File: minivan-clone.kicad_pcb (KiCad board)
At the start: 2 copper layers, 247.4 x 75.9 mm, 116 parts, among them CON101 HRO-TYPE-C-31-M-12, K101 KEYSW, K102 KEYSW, K103 KEYSW, K104 KEYSW, K105 KEYSW, K106 KEYSW, K107 KEYSW, K108 KEYSW, K110 KEYSW, K111 KEYSW, K112 KEYSW, K113 KEYSW, K114 KEYSW, K115 KEYSW, K116 KEYSW, K117 KEYSW, K118 KEYSW, K119 KEYSW, K120 KEYSW, K121 KEYSW, K122 KEYSW, K123 KEYSW, K124 KEYSW, K125 KEYSW, K126 KEYSW, K127 KEYSW, K128 KEYSW, K129 KEYSW, K130 KEYSW, K131 KEYSW, K132 KEYSW, K133 KEYSW, K134 KEYSW, K135 KEYSW, K136 KEYSW, K137 KEYSW, K138 KEYSW, K139 KEYSW, K140 KEYSW, K141 KEYSW, K142 KEYSW, K143 KEYSW, K144 KEYSW, K145 KEYSW, K146 KEYSW, K147 KEYSW, K148 KEYSW, SW101 SW_PUSH, U101 ATMEGA32U2, X101 XTAL_GND

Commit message: added icon to pcb
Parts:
- added G***: LOGO, icon:icon, F.Cu at (345.9, 165.1)
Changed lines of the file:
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@@
     (tracks 863)
     (zones 0)
-    (modules 116)
+    (modules 117)
     (nets 84)
   )
@@
     (add_net "Net-(R102-Pad1)")
   )
+  (module icon:icon (layer F.Cu)
+    (at 345.948 165.1)
+    (fp_text reference G*** (at 0 0) (layer F.SilkS) hide
+      (effects (font (size 1.524 1.524) (thickness 0.3)))
+    )
+    (fp_text value LOGO (at 0.75 0) (layer F.SilkS) hide
+      (effects (font (size 1.524 1.524) (thickness 0.3)))
+    )
+    (fp_poly (pts (xy -16.681691 0.453633) (xy -16.67213 1.32069) (xy -16.395957 2.129268) (xy -15.885356 2.816868)
+      (xy -15.216434 3.299082) (xy -14.794581 3.57815) (xy -14.668687 3.834571) (xy -14.671541 3.855207)
+      (xy -14.842051 4.080963) (xy -15.185572 4.143386) (xy -15.624922 4.042535) (xy -15.979205 3.854169)
+      (xy -16.385945 3.485206) (xy -16.734086 3.020855) (xy -16.778041 2.941403) (xy -16.985788 2.316247)
+      (xy -17.061288 1.584014) (xy -17.002025 0.87235) (xy -16.829138 0.350734) (xy -16.600536 -0.074706)
+      (xy -16.681691 0.453633)) (layer Eco2.User) (width 0.01))
+    (fp_poly (pts (xy 8.827697 -3.648363) (xy 9.045453 -3.521941) (xy 9.243273 -3.305469) (xy 9.192998 -3.067425)
+      (xy 9.173564 -3.034339) (xy 8.911681 -2.792098) (xy 8.593301 -2.716115) (xy 8.333057 -2.820437)
+      (xy 8.267906 -2.923358) (xy 8.265608 -3.265696) (xy 8.44141 -3.581057) (xy 8.607893 -3.691062)
+      (xy 8.827697 -3.648363)) (layer Eco2.User) (width 0.01))
+    (fp_poly (pts (xy -0.177583 -3.642129) (xy -0.048558 -3.564181) (xy 0.107123 -3.282951) (xy 0.119269 -3.076015)
+      (xy -0.040312 -2.811696) (xy -0.337821 -2.714246) (xy -0.64642 -2.811993) (xy -0.725358 -2.887381)
+      (xy -0.833872 -3.192888) (xy -0.726542 -3.47272) (xy -0.481677 -3.648569) (xy -0.177583 -3.642129)) (layer Eco2.User) (width 0.01))
+    (fp_poly (pts (xy 11.243235 -1.616568) (xy 11.545267 -1.447253) (xy 11.625766 -1.243258) (xy 11.67212 -0.917693)
+      (xy 12.20691 -1.280611) (xy 12.889803 -1.582854) (xy 13.622875 -1.639094) (xy 14.323873 -1.456975)
+      (xy 14.910544 -1.044138) (xy 14.925771 -1.027997) (xy 15.237885 -0.692982) (xy 15.575119 -1.000173)
+      (xy 16.265855 -1.452416) (xy 17.026616 -1.648439) (xy 17.792864 -1.580315) (xy 18.349285 -1.340875)
+      (xy 18.711707 -1.060091) (xy 18.970212 -0.696074) (xy 19.139809 -0.199258) (xy 19.235508 0.479923)
+      (xy 19.272315 1.391035) (xy 19.274118 1.713437) (xy 19.274118 3.436471) (xy 18.527059 3.436471)
+      (xy 18.527059 1.802668) (xy 18.512977 0.903898) (xy 18.460201 0.251592) (xy 18.352937 -0.205728)
+      (xy 18.175389 -0.519542) (xy 17.911764 -0.74133) (xy 17.713869 -0.847765) (xy 17.298857 -1.001579)
+      (xy 16.920113 -0.999688) (xy 16.606378 -0.920616) (xy 16.171125 -0.746652) (xy 15.858211 -0.494362)
+      (xy 15.646158 -0.115521) (xy 15.513487 0.438099) (xy 15.438719 1.214724) (xy 15.414454 1.755589)
+      (xy 15.387388 2.482697) (xy 15.356902 2.96251) (xy 15.31032 3.246411) (xy 15.234963 3.385783)
+      (xy 15.118155 3.432013) (xy 14.999757 3.436471) (xy 14.642353 3.436471) (xy 14.642353 1.594868)
+      (xy 14.638825 0.818389) (xy 14.622062 0.282298) (xy 14.582799 -0.07181) (xy 14.511768 -0.302343)
+      (xy 14.399703 -0.46771) (xy 14.298994 -0.569303) (xy 13.738257 -0.911922) (xy 13.111446 -0.970254)
+      (xy 12.552667 -0.790273) (xy 12.191451 -0.563261) (xy 11.940269 -0.279291) (xy 11.780331 0.116578)
+      (xy 11.692842 0.679285) (xy 11.659013 1.463769) (xy 11.65632 1.830294) (xy 11.654118 3.436471)
+      (xy 10.907059 3.436471) (xy 10.907059 -1.664313) (xy 11.243235 -1.616568)) (layer Eco2.User) (width 0.01))
+    (fp_poly (pts (xy 8.703235 -1.616568) (xy 8.826555 -1.589886) (xy 8.91615 -1.52162) (xy 8.978373 -1.368815)
+      (xy 9.019577 -1.088513) (xy 9.046113 -0.637758) (xy 9.064334 0.026408) (xy 9.080377 0.933824)
+      (xy 9.121343 3.436471) (xy 8.367059 3.436471) (xy 8.367059 -1.664313) (xy 8.703235 -1.616568)) (layer Eco2.User) (width 0.01))
+    (fp_poly (pts (xy 4.839744 -1.607871) (xy 5.514634 -1.393295) (xy 6.060742 -0.988591) (xy 6.205479 -0.804796)
+      (xy 6.332183 -0.56914) (xy 6.421616 -0.263497) (xy 6.482506 0.171332) (xy 6.523577 0.794542)
+      (xy 6.549848 1.531471) (xy 6.604127 3.436471) (xy 5.827059 3.436471) (xy 5.827059 1.785522)
+      (xy 5.805722 0.851933) (xy 5.731181 0.168967) (xy 5.587639 -0.309226) (xy 5.359297 -0.628498)
+      (xy 5.03036 -0.834697) (xy 4.908007 -0.881954) (xy 4.202056 -0.981401) (xy 3.5353 -0.796729)
+      (xy 3.041026 -0.42536) (xy 2.857022 -0.2186) (xy 2.733197 -0.011907) (xy 2.655054 0.259862)
+      (xy 2.608097 0.661846) (xy 2.577831 1.25919) (xy 2.562008 1.727232) (xy 2.536595 2.461524)
+      (xy 2.507662 2.948092) (xy 2.462827 3.237904) (xy 2.389706 3.381927) (xy 2.275917 3.431129)
+      (xy 2.146732 3.436471) (xy 1.785716 3.436471) (xy 1.826681 0.933824) (xy 1.842925 0.016723)
+      (xy 1.86121 -0.644543) (xy 1.887888 -1.092929) (xy 1.929313 -1.371393) (xy 1.991836 -1.522891)
+      (xy 2.081809 -1.590381) (xy 2.203824 -1.616568) (xy 2.440648 -1.604772) (xy 2.530158 -1.422512)
+      (xy 2.54 -1.205686) (xy 2.54 -0.747058) (xy 2.84479 -1.051849) (xy 3.424583 -1.443047)
+      (xy 4.116314 -1.626422) (xy 4.839744 -1.607871)) (layer Eco2.User) (width 0.01))
+    (fp_poly (pts (xy 0 3.436471) (xy -0.754284 3.436471) (xy -0.713319 0.933824) (xy -0.697075 0.016723)
+      (xy -0.67879 -0.644543) (xy -0.652112 -1.092929) (xy -0.610687 -1.371393) (xy -0.548164 -1.522891)
+      (xy -0.458191 -1.590381) (xy -0.336176 -1.616568) (xy 0 -1.664313) (xy 0 3.436471)) (layer Eco2.User) (width 0.01))
+    (fp_poly (pts (xy -2.689412 3.436471) (xy -3.429414 3.436471) (xy -3.511176 -1.666717) (xy -4.715852 0.399289)
+      (xy -5.245498 1.283734) (xy -5.655245 1.912732) (xy -5.954895 2.300043) (xy -6.15425 2.459427)
+      (xy -6.18764 2.465294) (xy -6.364884 2.35727) (xy -6.641047 2.024186) (xy -7.025774 1.452527)
+      (xy -7.52871 0.628776) (xy -7.672377 0.384715) (xy -8.89 -1.695864) (xy -8.930881 0.870303)
+      (xy -8.971762 3.436471) (xy -9.711765 3.436471) (xy -9.711765 -3.287058) (xy -9.338235 -3.287058)
+      (xy -9.056538 -3.248601) (xy -8.962901 -3.175) (xy -8.889779 -3.016482) (xy -8.687649 -2.643945)
+      (xy -8.380564 -2.100017) (xy -7.992577 -1.427325) (xy -7.567592 -0.702117) (xy -6.174088 1.658706)
+      (xy -4.767001 -0.776823) (xy -4.235785 -1.683008) (xy -3.823015 -2.353443) (xy -3.508403 -2.817045)
+      (xy -3.27166 -3.102729) (xy -3.092499 -3.239412) (xy -3.024663 -3.260097) (xy -2.689412 -3.307842)
+      (xy -2.689412 3.436471)) (layer Eco2.User) (width 0.01))
+    (fp_poly (pts (xy -14.568776 -4.62186) (xy -14.3259 -4.281572) (xy -14.124906 -3.838725) (xy -13.87114 -3.296724)
+      (xy -13.512815 -2.633662) (xy -13.117432 -1.972795) (xy -13.020249 -1.821666) (xy -12.302012 -0.642739)
+      (xy -11.813422 0.347974) (xy -11.553612 1.152416) (xy -11.506999 1.568824) (xy -11.635856 2.568751)
+      (xy -12.003777 3.43356) (xy -12.579462 4.130537) (xy -13.331612 4.626966) (xy -14.228927 4.890134)
+      (xy -14.717059 4.924026) (xy -15.308198 4.865366) (xy -15.894256 4.718332) (xy -16.063046 4.651938)
+      (xy -16.840694 4.144837) (xy -17.423291 3.447135) (xy -17.790237 2.610852) (xy -17.920932 1.688002)
+      (xy -17.917854 1.664641) (xy -17.446716 1.664641) (xy -17.393163 2.13026) (xy -17.328482 2.402781)
+      (xy -17.024117 3.189498) (xy -16.56944 3.761459) (xy -15.951163 4.167077) (xy -15.241653 4.423681)
+      (xy -14.531585 4.458297) (xy -13.858449 4.325226) (xy -13.243951 4.021566) (xy -12.681137 3.509255)
+      (xy -12.255511 2.876547) (xy -12.116063 2.526842) (xy -12.00321 1.743345) (xy -12.127327 0.900716)
+      (xy -12.496408 -0.028991) (xy -13.118445 -1.073719) (xy -13.165781 -1.143293) (xy -13.450559 -1.588022)
+      (xy -13.801222 -2.176184) (xy -14.145476 -2.786257) (xy -14.170076 -2.831453) (xy -14.749482 -3.899261)
+      (xy -14.945556 -3.425898) (xy -15.109665 -3.09533) (xy -15.389827 -2.595293) (xy -15.739594 -2.007091)
+      (xy -15.952616 -1.663032) (xy -16.54003 -0.705595) (xy -16.967043 0.058303) (xy -17.24976 0.67625)
+      (xy -17.404283 1.195834) (xy -17.446716 1.664641) (xy -17.917854 1.664641) (xy -17.794775 0.730604)
+      (xy -17.715923 0.47836) (xy -17.54777 0.10488) (xy -17.257644 -0.438228) (xy -16.889371 -1.071979)
+      (xy -16.565594 -1.594836) (xy -16.14842 -2.27509) (xy -15.75766 -2.959066) (xy -15.444426 -3.554819)
+      (xy -15.292644 -3.884706) (xy -15.032384 -4.422648) (xy -14.797682 -4.668626) (xy -14.568776 -4.62186)) (layer Eco2.User) (width 0.01))
+  )
   (module keebs:Mx_Alps_100 (layer F.Cu)

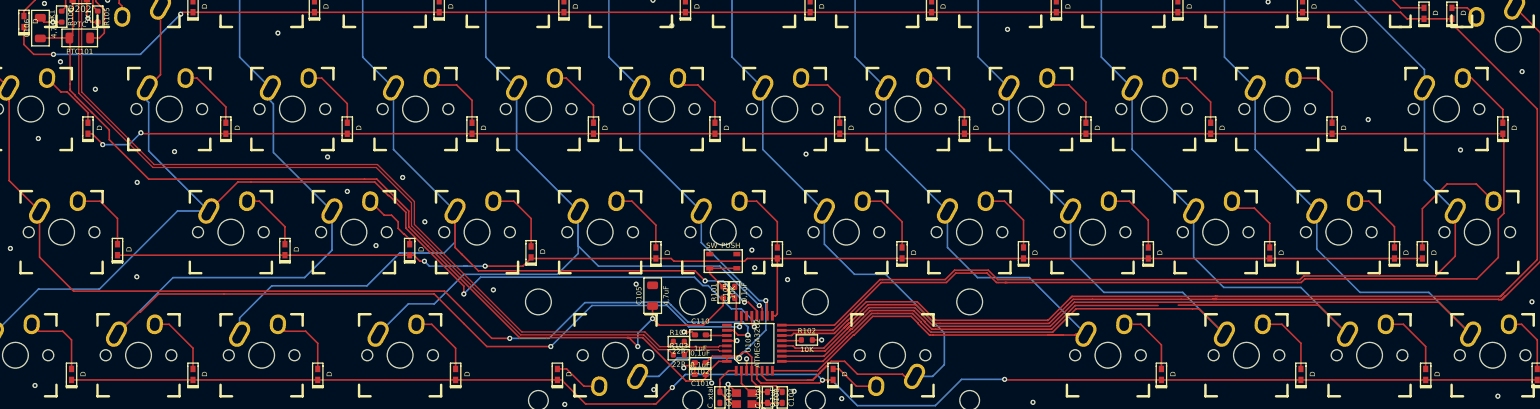
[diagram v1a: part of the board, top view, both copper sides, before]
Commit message: added mounting holes
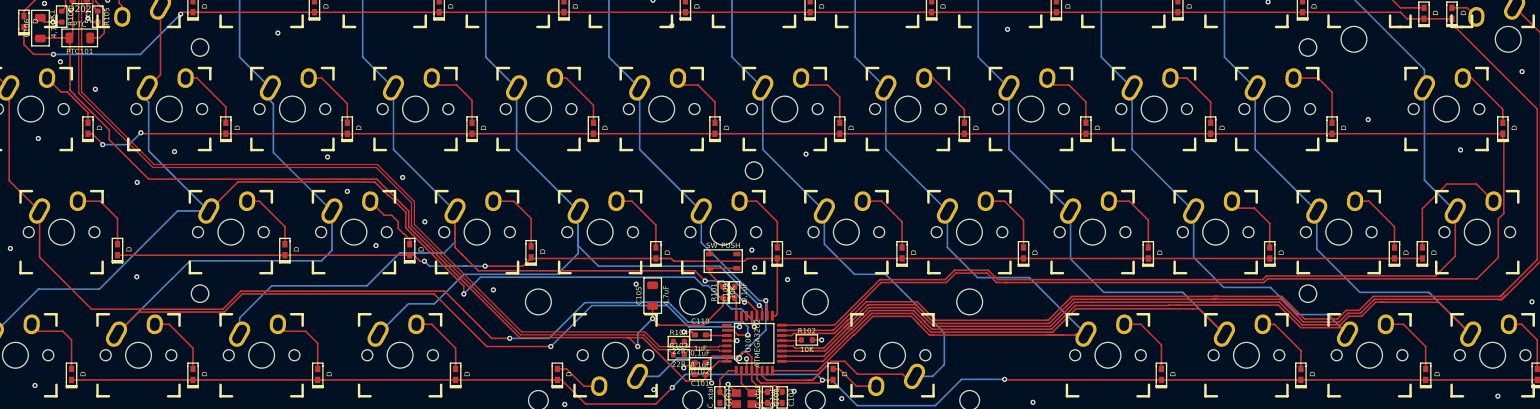
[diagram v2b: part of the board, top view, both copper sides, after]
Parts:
- added H1: MountingHole_2.7mm_M2.5, MountingHole:MountingHole_2.7mm_M2.5, F.Cu at (158.6, 147.5)
- added H2: MountingHole_2.7mm_M2.5, MountingHole:MountingHole_2.7mm_M2.5, F.Cu at (158.6, 185.6)
- added H3: MountingHole_2.7mm_M2.5, MountingHole:MountingHole_2.7mm_M2.5, F.Cu at (330.0, 147.5)
- added H4: MountingHole_2.7mm_M2.5, MountingHole:MountingHole_2.7mm_M2.5, F.Cu at (330.0, 185.6)
- added H5: MountingHole_2.7mm_M2.5, MountingHole:MountingHole_2.7mm_M2.5, F.Cu at (244.3, 166.6)
- moved G*** 1.02 mm to (344.9, 165.1)
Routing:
- net /PD5: track 193.9 -> 197.2 mm
- net /PD4: track 172.3 -> 175.5 mm
- net /PB0: track 396.1 -> 399.0 mm
- net /PD6: track 168.9 -> 171.8 mm
- net /PC4: track 171.7 -> 174.0 mm
- net Net-(D145-Pad2): track 11.1 -> 10.6 mm
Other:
- board text added: "rev 1"

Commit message: fixed DRC errors
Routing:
- net /PB1: track 357.5 -> 358.3 mm
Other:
- outline, holes or cut-outs redrawn

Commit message: started mirroring keyboard layout
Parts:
- moved C106 209.6 mm to (343.4, 144.5)
- moved D202 209.6 mm to (349.5, 139.2)
- moved PTC101 209.6 mm to (349.5, 146.1)
- moved R105 209.6 mm to (352.3, 142.7)
- moved >NAME 209.5 mm to (139.5, 138.0)
- moved CON101 209.5 mm to (349.1, 127.0)
- moved R106 209.5 mm to (346.7, 142.7)
- renumbered K114 to K101, K113 to K102, K112 to K103, K111 to K104, K110 to K105, K108 to K106, K106 to K108, K105 to K109, K104 to K110, K103 to K111, K102 to K112, K101 to K113, K126 to K114, K125 to K115, K124 to K116, K123 to K118, K122 to K119, K121 to K120, K120 to K121, K119 to K122, K118 to K123, K117 to K124, K116 to K125, K115 to K126, K138 to K127, K137 to K128, K136 to K129, K135 to K130, K134 to K131, K133 to K132, K132 to K133, K131 to K134, K130 to K135, K129 to K136, K128 to K137, K127 to K138, K148 to K139, K147 to K140, K146 to K141, K145 to K142, K144 to K143, K143 to K144, K142 to K145, K141 to K146, K140 to K147, K139 to K148
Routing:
- net /pre_D-: track 135.6 -> 1.12 mm
- net /pre_D+: track 134.7 -> 1.12 mm
- net +5V: track 184.4 -> 113.3 mm
- net Net-(CON101-Pad11): track 21.9 -> 0.00 mm
- net GND: track 32.6 -> 20.5 mm, vias 48 -> 37
- net Net-(CON101-Pad4): track 7.68 -> 0.00 mm
- net Net-(CON101-Pad10): track 6.96 -> 0.00 mm
- net (no net): track 0.00 -> 4.32 mm
- net /PB2: track 171.9 -> 175.0 mm
- net Net-(D112-Pad2): track 24.1 -> 25.4 mm

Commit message: fixed staggering, rotated cpu, removed all tracks, started redoing tracks
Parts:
- K114, K138: footprint keebs:Mx_Alps_175 -> keebs:Mx_Alps_125
- K126, K127: footprint keebs:Mx_Alps_125 -> keebs:Mx_Alps_175
- moved D112 16.0 mm to (332.0, 141.2)
- moved D113 14.2 mm to (366.3, 145.0)
- moved K115 9.53 mm to (334.8, 157.1)
- moved K116 9.53 mm to (315.7, 157.1)
- moved K128 9.53 mm to (325.3, 176.1)
- moved K129 9.53 mm to (306.2, 176.1)
- moved K121 9.53 mm to (239.5, 157.1)
- moved K122 9.53 mm to (220.5, 157.1)
- moved K123 9.53 mm to (201.4, 157.1)
- moved K125 9.53 mm to (163.3, 157.1)
- moved K133 9.53 mm to (230.0, 176.1)
- moved K134 9.53 mm to (211.0, 176.1)
- moved K135 9.53 mm to (191.9, 176.1)
- moved K137 9.53 mm to (153.8, 176.1)
- moved K118 9.52 mm to (296.7, 157.1)
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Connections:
- >NAME pad 1: /PB2 -> /PC4
- >NAME pad 2: Net-(D112-Pad2) -> Net-(D101-Pad2)
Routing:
- net /PB1: track 358.3 -> 0.00 mm, vias 2 -> 0
- net /PC2: track 247.5 -> 12.8 mm, vias 3 -> 0
- net /PB3: track 213.6 -> 0.00 mm, vias 2 -> 0
- net /PB0: track 399.0 -> 199.6 mm, vias 2 -> 0
- net /PD5: track 197.2 -> 0.00 mm
- net /PC6: track 197.0 -> 0.00 mm, vias 2 -> 0
- net /PB7: track 179.8 -> 0.00 mm, vias 2 -> 0
- net /PD4: track 175.5 -> 0.00 mm
- net /pre_D-: track 1.12 -> 176.2 mm
- net /PB2: track 175.0 -> 0.00 mm
- net /PC4: track 174.0 -> 0.00 mm, vias 2 -> 0
- net /pre_D+: track 1.12 -> 175.1 mm
- net /PD6: track 171.8 -> 0.00 mm
- net /PD3: track 155.9 -> 0.00 mm
- net /PB6: track 147.2 -> 0.00 mm, vias 2 -> 0
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
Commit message: started adding tracks
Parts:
- moved D137 12.4 mm to (360.2, 179.3)
- moved D132 11.9 mm to (255.3, 179.3)
- moved D130 10.4 mm to (218.7, 178.8)
- moved D125 10.4 mm to (349.8, 160.0)
- moved D129 9.53 mm to (200.3, 178.8)
- moved D121 9.53 mm to (267.3, 160.0)
- moved D122 9.53 mm to (286.1, 160.0)
- moved D133 9.53 mm to (276.5, 179.3)
- moved D136 9.53 mm to (333.9, 179.3)
- moved D115 9.53 mm to (153.0, 160.0)
- moved D116 9.53 mm to (171.8, 160.0)
- moved D117 9.53 mm to (191.1, 160.0)
- moved D119 9.53 mm to (228.7, 160.0)
- moved D127 9.53 mm to (162.2, 178.8)
- moved D128 9.53 mm to (181.5, 178.8)
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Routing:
- net /PB3: track 0.00 -> 215.4 mm, vias 0 -> 2
- net /PB1: track 0.00 -> 204.1 mm, vias 0 -> 2
- net /PC4: track 0.00 -> 179.1 mm
- net /PB2: track 0.00 -> 52.0 mm
- net GND: track 16.6 -> 55.3 mm, vias 2 -> 7
- net /PB0: track 199.6 -> 237.7 mm, vias 0 -> 2
- net /RST: track 0.00 -> 20.7 mm, vias 0 -> 2
- net Net-(D131-Pad2): track 0.00 -> 16.3 mm
- net /PB7: track 0.00 -> 15.6 mm
- net Net-(D126-Pad2): track 0.00 -> 13.7 mm
- net Net-(D125-Pad2): track 0.00 -> 13.1 mm, vias 0 -> 1
- net /PC2: track 12.8 -> 1.41 mm
- net Net-(D113-Pad2): track 0.00 -> 10.8 mm
- net Net-(D127-Pad2): track 0.00 -> 9.87 mm
- net Net-(D137-Pad2): track 0.00 -> 9.73 mm
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
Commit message: more tracks for leftmost cols
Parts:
- moved R104 22.9 mm to (255.3, 196.8), turned to 180 degrees
- moved R103 22.6 mm to (255.3, 194.8), turned to 180 degrees
- moved R102 17.6 mm to (235.5, 197.1), turned to 180 degrees
- moved C101 17.2 mm to (252.0, 191.8), turned to 0 degrees
- moved C110 17.0 mm to (251.9, 197.9), turned to 180 degrees
- moved C107 16.7 mm to (248.9, 188.2), turned to 90 degrees
- moved C103 16.4 mm to (239.3, 188.2), turned to 90 degrees
- moved C102 16.2 mm to (252.0, 193.6), turned to 0 degrees
- moved C108 14.3 mm to (241.6, 188.2), turned to 90 degrees
- moved X101 14.0 mm to (245.1, 188.0), turned to 180 degrees
- moved C105 4.26 mm to (229.9, 181.9)
- moved D143 3.42 mm to (258.8, 200.7)
- moved U101 3.39 mm to (243.6, 196.6), turned to 270 degrees
- moved R101 2.27 mm to (234.4, 181.4), turned to 0 degrees
- moved C109 1.83 mm to (234.4, 183.1), turned to 0 degrees
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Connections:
- D126 pad 1: /PB3 -> /PC2
- D127 pad 1: /PB3 -> /PC2
- D128 pad 1: /PB3 -> /PC2
- D129 pad 1: /PB3 -> /PC2
- D130 pad 1: /PB3 -> /PC2
- D131 pad 1: /PB3 -> /PC2
- D132 pad 1: /PB3 -> /PC2
- D133 pad 1: /PB3 -> /PC2
- D134 pad 1: /PB3 -> /PC2
- D135 pad 1: /PB3 -> /PC2
- D136 pad 1: /PB3 -> /PC2
- D137 pad 1: /PB3 -> /PC2
- D138 pad 1: /PC2 -> /PB3
- D139 pad 1: /PC2 -> /PB3
- D140 pad 1: /PC2 -> /PB3
- D141 pad 1: /PC2 -> /PB3
- D142 pad 1: /PC2 -> /PB3
- D143 pad 1: /PC2 -> /PB3
- D144 pad 1: /PC2 -> /PB3
- D145 pad 1: /PC2 -> /PB3
- D146 pad 1: /PC2 -> /PB3
- D147 pad 1: /PC2 -> /PB3
- K102 pad 1: /PB2 -> /PB4
- K108 pad 1: /PB4 -> /PB2
- K114 pad 1: /PB2 -> /PB4
- K121 pad 1: /PB4 -> /PB2
- K127 pad 1: /PB2 -> /PB4
- K133 pad 1: /PB4 -> /PB2
- K144 pad 1: /PB4 -> /PB2
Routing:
- net /PC2: track 1.41 -> 215.4 mm, vias 0 -> 2
- net /PB7: track 15.6 -> 105.0 mm, vias 0 -> 2
- net /PC6: track 0.00 -> 69.8 mm, vias 0 -> 2
- net /PC4: track 179.1 -> 110.0 mm
- net /PB4: track 0.00 -> 52.0 mm
- net /PB2: track 52.0 -> 0.00 mm
- net /PB6: track 0.00 -> 50.6 mm, vias 0 -> 2
- net /PB5: track 0.00 -> 31.7 mm, vias 0 -> 2
- net /pre_D-: track 176.2 -> 150.4 mm
- net /pre_D+: track 175.1 -> 152.0 mm
- net /PB3: track 215.4 -> 236.3 mm, vias 2 -> 0
- net /RST: track 20.7 -> 31.4 mm
- net +5V: track 35.7 -> 45.7 mm
- net GND: track 55.3 -> 46.3 mm, vias 7 -> 10
- net Net-(C107-Pad1): track 10.9 -> 8.04 mm

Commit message: more tracks
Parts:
- moved D115 19.1 mm to (172.1, 160.0)
- moved D116 19.1 mm to (190.9, 160.0)
- moved D117 19.1 mm to (210.2, 160.0)
- moved D120 19.1 mm to (267.1, 160.0)
- moved D121 19.1 mm to (286.4, 160.0)
- moved D122 19.1 mm to (305.2, 160.0)
- moved D123 19.1 mm to (324.5, 160.0)
- moved D124 19.1 mm to (343.3, 160.0)
- moved D118 19.0 mm to (229.0, 160.0)
- moved D119 19.0 mm to (247.8, 160.0)
- moved D125 14.7 mm to (364.5, 160.0)
- moved D126 5.08 mm to (140.7, 178.8)
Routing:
- net /PD3: track 0.00 -> 91.1 mm
- net /PD5: track 0.00 -> 91.1 mm
- net /PD4: track 0.00 -> 91.1 mm
- net /PD2: track 0.00 -> 88.7 mm
- net /PB6: track 50.6 -> 103.0 mm, vias 2 -> 1
- net /PC6: track 69.8 -> 121.1 mm, vias 2 -> 1
- net /PB2: track 0.00 -> 48.0 mm
- net /PD0: track 0.00 -> 48.0 mm
- net /PB5: track 31.7 -> 48.0 mm, vias 2 -> 0
- net /PB1: track 204.1 -> 218.8 mm
- net /PC4: track 110.0 -> 122.4 mm
- net Net-(D140-Pad2): track 0.00 -> 9.46 mm
- net Net-(D138-Pad2): track 0.00 -> 9.46 mm
- net Net-(D141-Pad2): track 0.00 -> 9.42 mm
- net Net-(D139-Pad2): track 0.00 -> 9.36 mm
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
